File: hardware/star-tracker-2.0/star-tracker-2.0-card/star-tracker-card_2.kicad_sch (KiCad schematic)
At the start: 88 parts, among them Q2 DMN3028LQ-7, Q3 DMP2240UDM, Q4 DMN3028LQ-7, Q5 DMP3050LVT-7, Q6 DMP3050LVT-7, U12 MIC842LYC5, U13 MIC842LYC5, U14 MAX4211FETE, U15 TPS62112, U16 MAX7310ATE, U2 TS5A21366DCUR

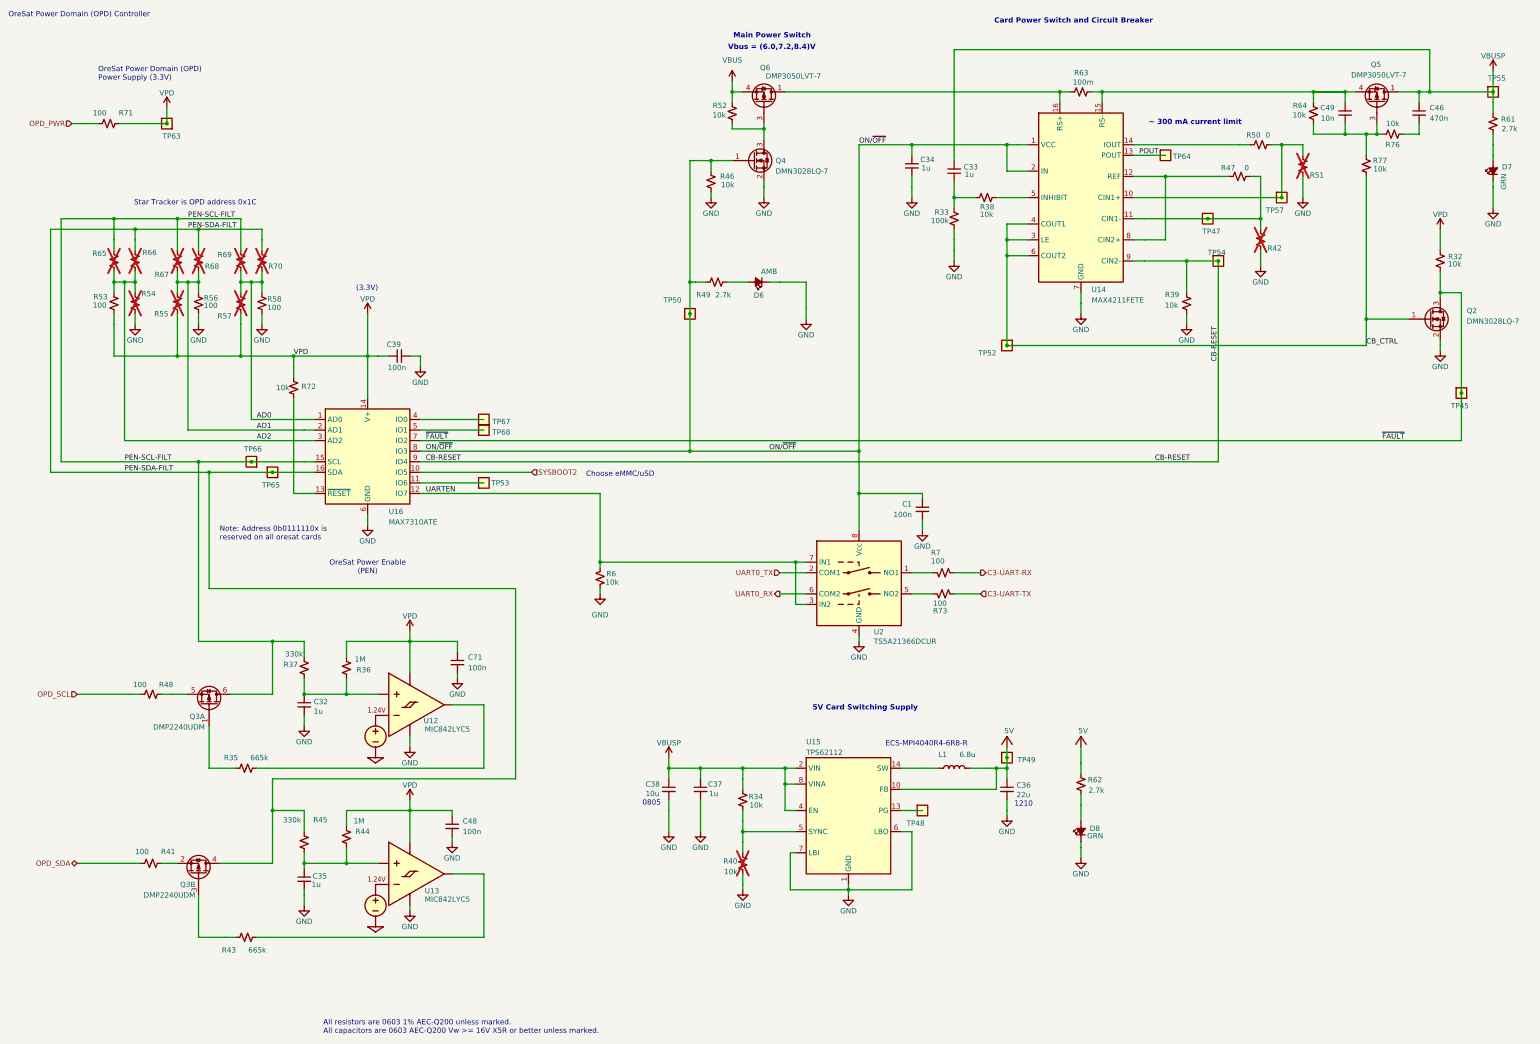
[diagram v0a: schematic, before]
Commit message: Star tracker board update
Added 3d models to footprints, reannotated component designators
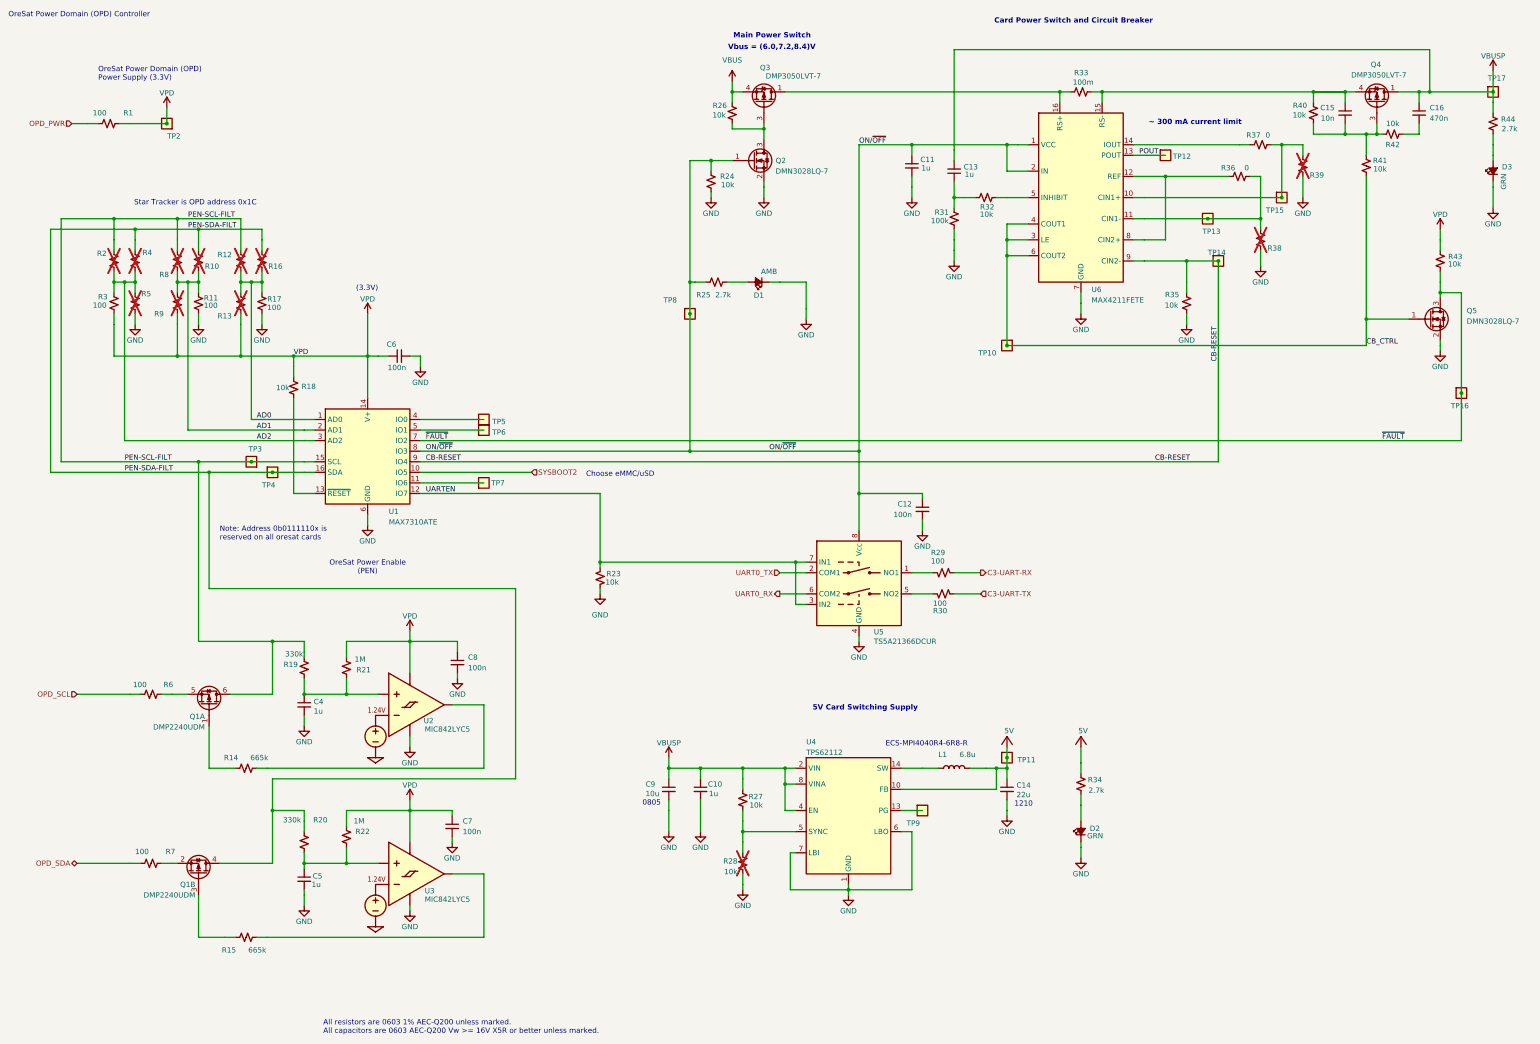
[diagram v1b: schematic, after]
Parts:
- renumbered C37 to C10, C34 to C11, C1 to C12, C33 to C13, C36 to C14, C49 to C15, C46 to C16, C32 to C4, C35 to C5, C39 to C6, C48 to C7, C71 to C8, C38 to C9, D6 to D1, D8 to D2, D7 to D3, Q3 to Q1, Q4 to Q2, Q6 to Q3, Q5 to Q4, Q2 to Q5, R71 to R1, R68 to R10, R56 to R11, R69 to R12, R57 to R13, R35 to R14, R43 to R15, R70 to R16, R58 to R17, R72 to R18, R37 to R19, R65 to R2, R45 to R20, R36 to R21, R44 to R22, R6 to R23, R46 to R24, R49 to R25, R52 to R26, R34 to R27, R40 to R28, R7 to R29, R53 to R3, R73 to R30, R33 to R31, R38 to R32, R63 to R33, R62 to R34, R39 to R35, R47 to R36, R50 to R37, R42 to R38, R51 to R39, R66 to R4, R64 to R40, R77 to R41, R76 to R42, R32 to R43, R61 to R44, R54 to R5, R48 to R6, R41 to R7, R67 to R8, R55 to R9, TP52 to TP10, TP49 to TP11, TP64 to TP12, TP47 to TP13, TP54 to TP14, TP57 to TP15, TP45 to TP16, TP55 to TP17, TP63 to TP2, TP66 to TP3, TP65 to TP4, TP67 to TP5, TP68 to TP6, TP53 to TP7, TP50 to TP8, TP48 to TP9, U16 to U1, U12 to U2, U13 to U3, U15 to U4, U2 to U5, U14 to U6

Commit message: Component linking
Linked components to 3d models
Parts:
- C9: DPN 490-GRT21BC71E106KE13KCT-ND -> 1276-CL21B106KAYQNNETR-ND; MFR Murata Electronics -> Samsung Electro-Mechanics; MPN GRT21BC71E106KE13K -> CL21B106KAYQNNE
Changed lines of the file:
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@@
 			)
 		)
-		(property "Datasheet" "https://search.murata.co.jp/Ceramy/image/img/A01X/G101/ENG/GRT21BC71E106KE13-01.pdf"
+		(property "Datasheet" "https://mm.digikey.com/Volume0/opasdata/d220001/medias/docus/7851/1276_CL21B1.pdf"
 			(at 195.58 207.01 0)
 			(hide yes)
@@
 			)
 		)
-		(property "Description" "10 µF ±10% 25V Ceramic Capacitor X7S 0805 (2012 Metric)"
+		(property "Description" "10 µF ±10% 25V Ceramic Capacitor X7R 0805 (2012 Metric)"
 			(at 195.58 207.01 0)
 			(hide yes)
@@
 			)
 		)
-		(property "DPN" "490-GRT21BC71E106KE13KCT-ND"
+		(property "DPN" "1276-CL21B106KAYQNNETR-ND"
 			(at 195.58 207.01 0)
 			(hide yes)
@@
 			)
 		)
-		(property "MFR" "Murata Electronics"
+		(property "MFR" "Samsung Electro-Mechanics"
 			(at 195.58 207.01 0)
 			(hide yes)
@@
 			)
 		)
-		(property "MPN" "GRT21BC71E106KE13K"
+		(property "MPN" "CL21B106KAYQNNE"
 			(at 195.58 207.01 0)
 			(hide yes)

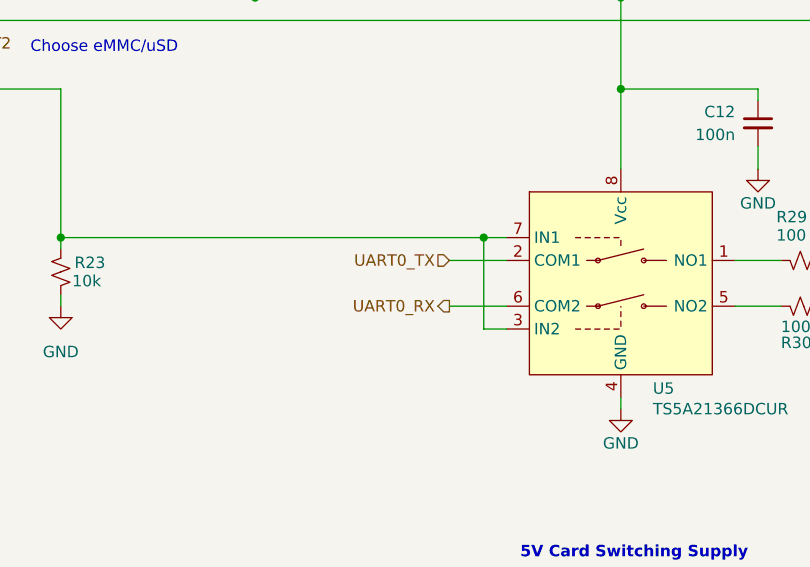
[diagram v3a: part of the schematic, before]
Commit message: Update to Camera Board
Update BOM for camera board, replaced lower tier dielectric caps to X7R
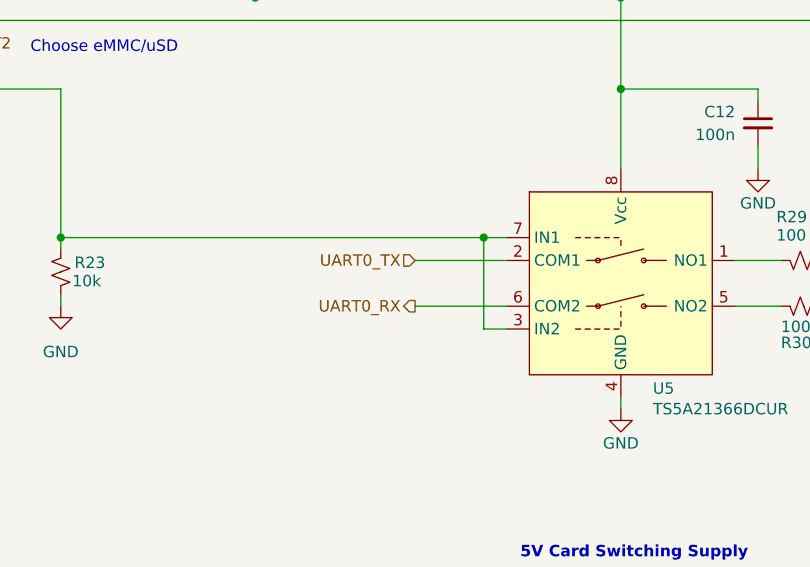
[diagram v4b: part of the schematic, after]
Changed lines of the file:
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@@
 	(wire
 		(pts
-			(xy 222.25 154.94) (xy 228.6 154.94)
+			(xy 218.44 154.94) (xy 228.6 154.94)
 		)
 		(stroke
@@
 	(wire
 		(pts
-			(xy 222.25 160.02) (xy 228.6 160.02)
+			(xy 218.44 160.02) (xy 228.6 160.02)
 		)
 		(stroke
@@
 	(hierarchical_label "UART0_RX"
 		(shape output)
-		(at 222.25 160.02 180)
+		(at 218.44 160.02 180)
 		(effects
 			(font
@@
 	(hierarchical_label "UART0_TX"
 		(shape input)
-		(at 222.25 154.94 180)
-		(effects
-			(font
+		(at 218.44 154.94 180)
+		(effects
+			(font

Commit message: Added extra Testpoints
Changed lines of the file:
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@@
 	)
 	(symbol
-		(lib_id "star-tracker-card-eagle-import:5V")
-		(at 276.86 194.31 0)
-		(unit 1)
-		(body_style 1)
-		(exclude_from_sim no)
-		(in_bom yes)
-		(on_board yes)
-		(in_pos_files yes)
-		(dnp no)
-		(property "Reference" "#3V-02"
-			(at 276.86 194.31 0)
-			(hide yes)
-			(show_name no)
-			(do_not_autoplace no)
-			(effects
-				(font
-					(size 1.27 1.27)
-				)
-			)
-		)
-		(property "Value" "5V"
-			(at 276.225 193.675 0)
-			(show_name no)
-			(do_not_autoplace no)
-			(effects
-				(font
-					(size 1.27 1.27)
-				)
-				(justify left bottom)
-			)
-		)
-		(property "Footprint" ""
-			(at 276.86 194.31 0)
-			(hide yes)
-			(show_name no)
-			(do_not_autoplace no)
-			(effects
-				(font
-					(size 1.27 1.27)
-				)
-			)
-		)
-		(property "Datasheet" ""
-			(at 276.86 194.31 0)
-			(hide yes)
-			(show_name no)
-			(do_not_autoplace no)
-			(effects
-				(font
-					(size 1.27 1.27)
-				)
-			)
-		)
-		(property "Description" ""
-			(at 276.86 194.31 0)
-			(hide yes)
-			(show_name no)
-			(do_not_autoplace no)
-			(effects
-				(font
-					(size 1.27 1.27)
-				)
-			)
-		)
-		(pin "1"
-		)
-		(instances
-			(project "star-tracker-card"
-				(path "/324e9eb5-7420-4b7e-862c-cc20bb28618a/79e6f5da-9b7e-4636-a735-d76e4a141190"
-					(reference "#3V-02")
-					(unit 1)
-				)
-			)
-		)
-	)
-	(symbol
 		(lib_id "star-tracker-card-eagle-import:VPD")
 		(at 381 72.39 0)
@@
 	)
 	(symbol
+		(lib_id "star-tracker-card-eagle-import:VDD")
+		(at 294.64 196.85 0)
+		(unit 1)
+		(body_style 1)
+		(exclude_from_sim no)
+		(in_bom yes)
+		(on_board yes)
+		(in_pos_files yes)
+		(dnp no)
+		(property "Reference" "#SUPPLY04"
+			(at 294.64 196.85 0)
+			(hide yes)
+			(show_name no)
+			(do_not_autoplace no)
+			(effects
+				(font
+					(size 1.27 1.27)
+				)
+			)
+		)
+		(property "Value" "5V"
+			(at 294.64 194.056 0)
+			(show_name no)
+			(do_not_autoplace no)
+			(effects
+				(font
+					(size 1.27 1.27)
+				)
+				(justify bottom)
+			)
+		)
+		(property "Footprint" ""
+			(at 294.64 196.85 0)
+			(hide yes)
+			(show_name no)
+			(do_not_autoplace no)
+			(effects
+				(font
+					(size 1.27 1.27)
+				)
+			)
+		)
+		(property "Datasheet" ""
+			(at 294.64 196.85 0)
+			(hide yes)
+			(show_name no)
+			(do_not_autoplace no)
+			(effects
+				(font
+					(size 1.27 1.27)
+				)
+			)
+		)
+		(property "Description" ""
+			(at 294.64 196.85 0)
+			(hide yes)
+			(show_name no)
+			(do_not_autoplace no)
+			(effects
+				(font
+					(size 1.27 1.27)
+				)
+			)
+		)
+		(pin "1"
+		)
+		(instances
+			(project "star-tracker-card"
+				(path "/324e9eb5-7420-4b7e-862c-cc20bb28618a/79e6f5da-9b7e-4636-a735-d76e4a141190"
+					(reference "#SUPPLY04")
+					(unit 1)
+				)
+			)
+		)
+	)
+	(symbol
 		(lib_id "power:GND")
 		(at 238.76 232.41 0)
@@
 	)
 	(symbol
+		(lib_id "star-tracker-card-eagle-import:VDD")
+		(at 276.86 196.85 0)
+		(unit 1)
+		(body_style 1)
+		(exclude_from_sim no)
+		(in_bom yes)
+		(on_board yes)
+		(in_pos_files yes)
+		(dnp no)
+		(property "Reference" "#SUPPLY03"
+			(at 276.86 196.85 0)
+			(hide yes)
+			(show_name no)
+			(do_not_autoplace no)
+			(effects
+				(font
+					(size 1.27 1.27)
+				)
+			)
+		)
+		(property "Value" "5V"
+			(at 276.86 194.056 0)
+			(show_name no)
+			(do_not_autoplace no)
+			(effects
+				(font
+					(size 1.27 1.27)
+				)
+				(justify bottom)
+			)
+		)
+		(property "Footprint" ""
+			(at 276.86 196.85 0)
+			(hide yes)
+			(show_name no)
+			(do_not_autoplace no)
+			(effects
+				(font
+					(size 1.27 1.27)
+				)
+			)
+		)
+		(property "Datasheet" ""
+			(at 276.86 196.85 0)
+			(hide yes)
+			(show_name no)
+			(do_not_autoplace no)
+			(effects
+				(font
+					(size 1.27 1.27)
+				)
+			)
+		)
+		(property "Description" ""
+			(at 276.86 196.85 0)
+			(hide yes)
+			(show_name no)
+			(do_not_autoplace no)
+			(effects
+				(font
+					(size 1.27 1.27)
+				)
+			)
+		)
+		(pin "1"
+		)
+		(instances
+			(project "star-tracker-card"
+				(path "/324e9eb5-7420-4b7e-862c-cc20bb28618a/79e6f5da-9b7e-4636-a735-d76e4a141190"
+					(reference "#SUPPLY03")
+					(unit 1)
+				)
+			)
+		)
+	)
+	(symbol
 		(lib_id "star-tracker-card-eagle-import:TEST-POINT")
 		(at 100.33 130.81 0)
@@
 					(unit 1)
 				)
-			)
-		)
-	)
-	(symbol
-		(lib_id "star-tracker-card-eagle-import:5V")
-		(at 294.64 194.31 0)
-		(unit 1)
-		(body_style 1)
-		(exclude_from_sim no)
-		(in_bom yes)
-		(on_board yes)
-		(in_pos_files yes)
-		(dnp no)
-		(property "Reference" "#3V-03"
-			(at 294.64 194.31 0)
-			(hide yes)
-			(show_name no)
-			(do_not_autoplace no)
-			(effects
-				(font
-					(size 1.27 1.27)
-				)
-			)
-		)
-		(property "Value" "5V"
-			(at 294.005 193.675 0)
-			(show_name no)
-			(do_not_autoplace no)
-			(effects
-				(font
-					(size 1.27 1.27)
-				)
-				(justify left bottom)
-			)
-		)
-		(property "Footprint" ""
-			(at 294.64 194.31 0)
-			(hide yes)
-			(show_name no)
-			(do_not_autoplace no)
-			(effects
-				(font
-					(size 1.27 1.27)
-				)
-			)
-		)
-		(property "Datasheet" ""
-			(at 294.64 194.31 0)
-			(hide yes)
-			(show_name no)
-			(do_not_autoplace no)
-			(effects
-				(font
-					(size 1.27 1.27)
-				)
-			)
-		)
-		(property "Description" ""
-			(at 294.64 194.31 0)
-			(hide yes)
-			(show_name no)
-			(do_not_autoplace no)
-			(effects
-				(font
-					(size 1.27 1.27)
-				)
-			)
-		)
-		(pin "1"
-		)
-		(instances
-			(project "star-tracker-card"
-				(path "/324e9eb5-7420-4b7e-862c-cc20bb28618a/79e6f5da-9b7e-4636-a735-d76e4a141190"
-					(reference "#3V-03")
-					(unit 1)
-				)
